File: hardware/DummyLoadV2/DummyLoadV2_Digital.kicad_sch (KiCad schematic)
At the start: 18 parts, among them J1 Conn_01x05_Pin, J2 Fan, Q3 2N7000, Q4 PMOS, SW1 Enable_SW, SW3 Range_SW, U1 Nano

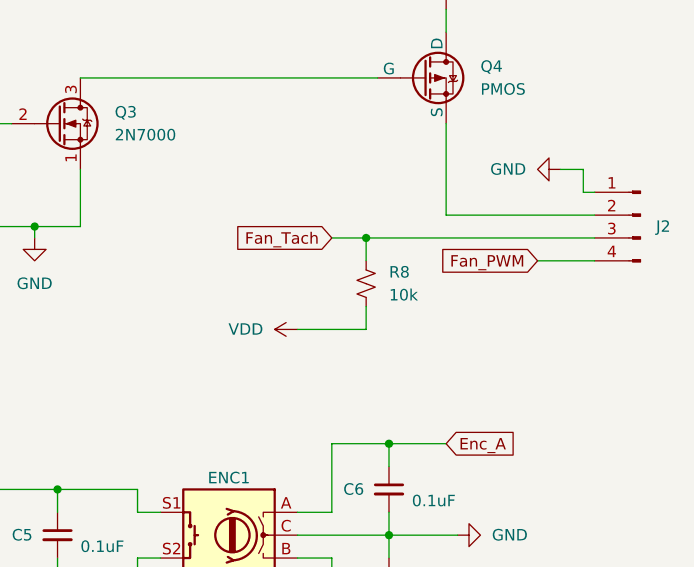
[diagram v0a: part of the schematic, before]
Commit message: Added hardware schematic sheets
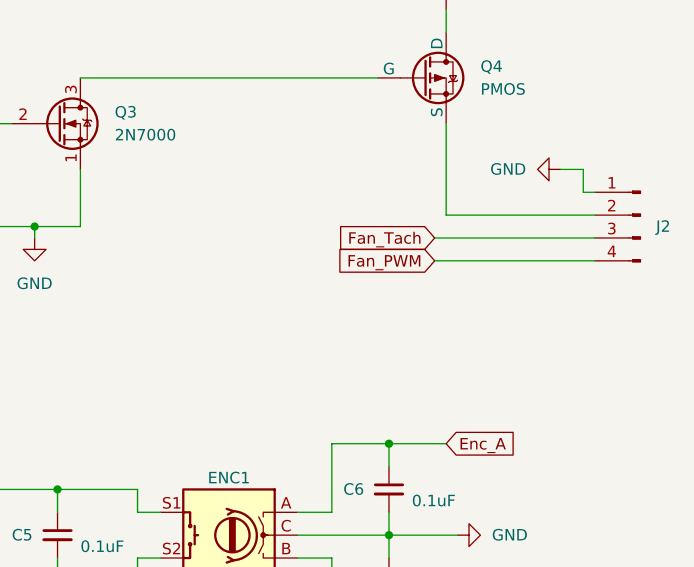
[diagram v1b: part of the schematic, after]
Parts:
- removed R8: 10k, symbol Device:R_Small_US
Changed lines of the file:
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@@
     (rev "1")
-  )
-  (junction (at 217.17 83.82) (diameter 0) (color 0 0 0 0)
   )
   (junction (at 74.93 132.08) (diameter 0) (color 0 0 0 0)
@@
     (stroke (width 0) (type default))
   )
-  (wire (pts (xy 213.36 83.82) (xy 217.17 83.82))
-    (stroke (width 0) (type default))
-  )
   (wire (pts (xy 191.77 111.76) (xy 191.77 114.3))
     (stroke (width 0) (type default))
@@
     (stroke (width 0) (type default))
   )
-  (wire (pts (xy 236.22 86.36) (xy 242.57 86.36))
-    (stroke (width 0) (type default))
-  )
   (wire (pts (xy 50.8 99.06) (xy 60.96 99.06))
     (stroke (width 0) (type default))
@@
     (stroke (width 0) (type default))
   )
-  (wire (pts (xy 217.17 83.82) (xy 217.17 86.36))
-    (stroke (width 0) (type default))
-  )
   (wire (pts (xy 241.3 78.74) (xy 242.57 78.74))
     (stroke (width 0) (type default))
@@
     (stroke (width 0) (type default))
   )
+  (wire (pts (xy 224.79 86.36) (xy 242.57 86.36))
+    (stroke (width 0) (type default))
+  )
   (wire (pts (xy 60.96 114.3) (xy 55.88 114.3))
     (stroke (width 0) (type default))
@@
     (stroke (width 0) (type default))
   )
-  (wire (pts (xy 217.17 83.82) (xy 242.57 83.82))
+  (wire (pts (xy 224.79 83.82) (xy 242.57 83.82))
     (stroke (width 0) (type default))
   )
@@
     (stroke (width 0) (type default))
   )
-  (wire (pts (xy 209.55 93.98) (xy 217.17 93.98))
-    (stroke (width 0) (type default))
-  )
   (wire (pts (xy 33.02 124.46) (xy 46.99 124.46))
     (stroke (width 0) (type default))
@@
   )
   (wire (pts (xy 219.71 116.84) (xy 227.33 116.84))
-    (stroke (width 0) (type default))
-  )
-  (wire (pts (xy 217.17 91.44) (xy 217.17 93.98))
     (stroke (width 0) (type default))
   )
@@
     )
   )
-  (global_label "Fan_PWM" (shape input) (at 236.22 86.36 180) (fields_autoplaced)
+  (global_label "Fan_PWM" (shape input) (at 224.79 86.36 180) (fields_autoplaced)
     (effects (font (size 1.27 1.27)) (justify right))
-    (property "Intersheetrefs" "${INTERSHEET_REFS}" (at 224.7078 86.36 0)
+    (property "Intersheetrefs" "${INTERSHEET_REFS}" (at 213.2778 86.36 0)
       (effects (font (size 1.27 1.27)) (justify right) hide)
     )
@@
     )
   )
-  (global_label "Fan_Tach" (shape input) (at 213.36 83.82 180) (fields_autoplaced)
+  (global_label "Fan_Tach" (shape input) (at 224.79 83.82 180) (fields_autoplaced)
     (effects (font (size 1.27 1.27)) (justify right))
-    (property "Intersheetrefs" "${INTERSHEET_REFS}" (at 201.6664 83.82 0)
+    (property "Intersheetrefs" "${INTERSHEET_REFS}" (at 213.0964 83.82 0)
       (effects (font (size 1.27 1.27)) (justify right) hide)
     )
@@
         (path "/154f9743-c032-4045-ba5f-d157ba47940d/02c25695-dda5-4c86-9b7a-9696a2c46048"
           (reference "NTC") (unit 1)
-        )
-      )
-    )
-  )
-  (symbol (lib_id "Device:R_Small_US") (at 217.17 88.9 0) (unit 1)
-    (in_bom yes) (on_board yes) (dnp no)
-    (property "Reference" "R8" (at 219.71 87.63 0)
-      (effects (font (size 1.27 1.27)) (justify left))
-    )
-    (property "Value" "10k" (at 219.71 90.17 0)
-      (effects (font (size 1.27 1.27)) (justify left))
-    )
-    (property "Footprint" "" (at 217.17 88.9 0)
-      (effects (font (size 1.27 1.27)) hide)
-    )
-    (property "Datasheet" "~" (at 217.17 88.9 0)
-      (effects (font (size 1.27 1.27)) hide)
-    )
-    (pin "1")
-    (pin "2")
-    (instances
-      (project "DummyLoadV2"
-        (path "/154f9743-c032-4045-ba5f-d157ba47940d/02c25695-dda5-4c86-9b7a-9696a2c46048"
-          (reference "R8") (unit 1)
         )
       )
@@
         )
       )
-    )
-  )
-  (symbol (lib_id "power:VDD") (at 209.55 93.98 90) (unit 1)
-    (in_bom yes) (on_board yes) (dnp no)
-    (property "Reference" "#PWR031" (at 213.36 93.98 0)
-      (effects (font (size 1.27 1.27)) hide)
-    )
-    (property "Value" "VDD" (at 205.74 93.98 90)
-      (effects (font (size 1.27 1.27)) (justify left))
-    )
-    (property "Footprint" "" (at 209.55 93.98 0)
-      (effects (font (size 1.27 1.27)) hide)
-    )
-    (property "Datasheet" "" (at 209.55 93.98 0)
-      (effects (font (size 1.27 1.27)) hide)
-    )
-    (pin "1")
-    (instances
-      (project "DummyLoadV2"
-        (path "/154f9743-c032-4045-ba5f-d157ba47940d/02c25695-dda5-4c86-9b7a-9696a2c46048"
-          (reference "#PWR031") (unit 1)
-        )
-      )

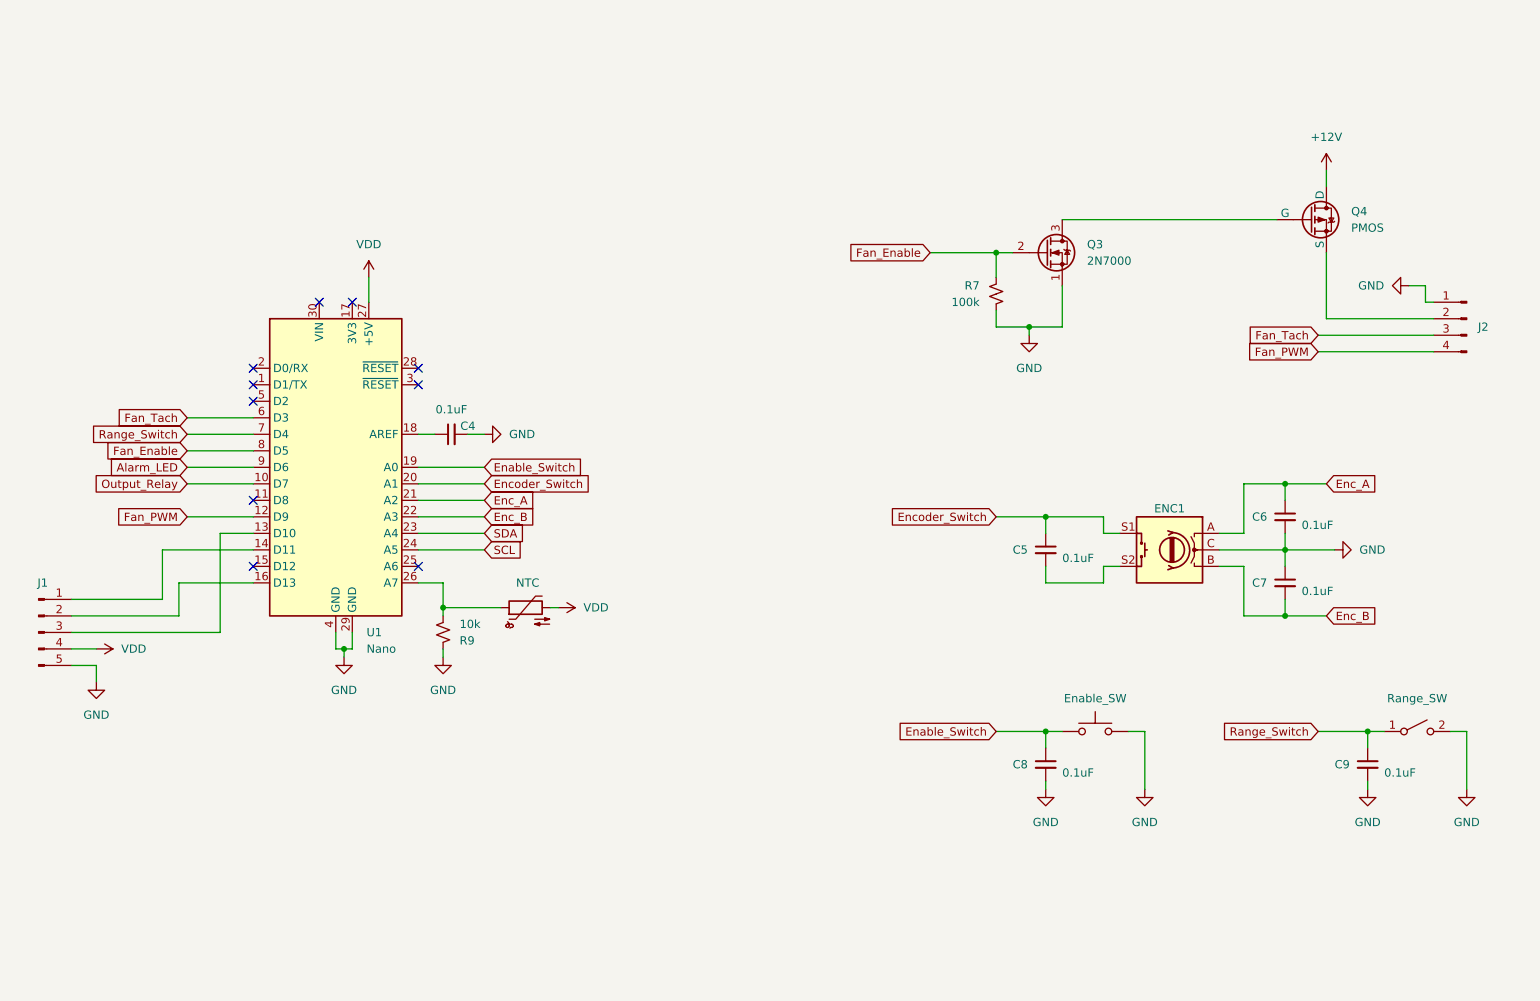
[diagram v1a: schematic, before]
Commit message: Updated pin mapping in schematic
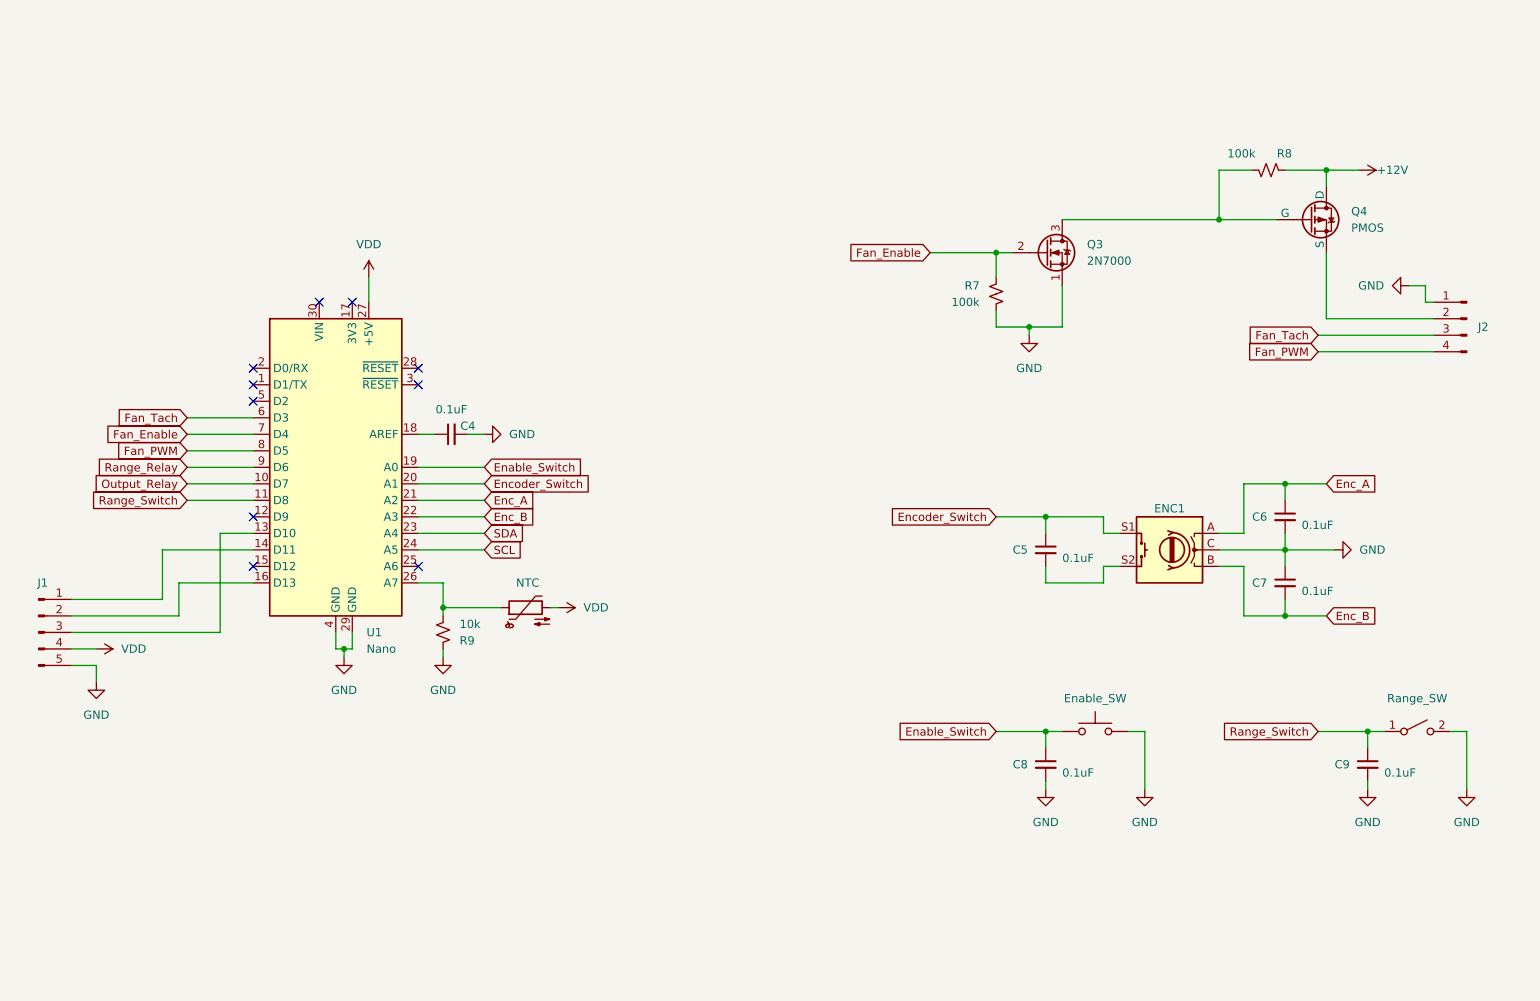
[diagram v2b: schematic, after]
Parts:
- added R8: 100k, symbol Device:R_Small_US
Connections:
- net +12V: now also R8.1
- net Fan_Enable: now also U1.7 (D4); no longer U1.8 (D5)
- net Fan_PWM: now also U1.8 (D5); no longer U1.12 (D9)
- net Range_Switch: now also U1.11 (D8); no longer U1.7 (D4)
- net at Q3.3 (D), Q4.2 (G): now also R8.2
- net Alarm_LED renamed Range_Relay
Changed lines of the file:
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@@
     (rev "1")
   )
+  (junction (at 209.55 66.04) (diameter 0) (color 0 0 0 0)
+  )
   (junction (at 74.93 132.08) (diameter 0) (color 0 0 0 0)
   )
@@
   (junction (at 182.88 111.76) (diameter 0) (color 0 0 0 0)
   )
+  (junction (at 226.06 58.42) (diameter 0) (color 0 0 0 0)
+  )
   (junction (at 182.88 144.78) (diameter 0) (color 0 0 0 0)
   )
@@
   )
   (no_connect (at 86.36 91.44))
+  (no_connect (at 60.96 111.76))
   (no_connect (at 71.12 78.74))
   (no_connect (at 86.36 88.9))
@@
   (no_connect (at 60.96 93.98))
   (no_connect (at 60.96 88.9))
-  (no_connect (at 60.96 109.22))
   (no_connect (at 76.2 78.74))
   (no_connect (at 86.36 119.38))
@@
     (stroke (width 0) (type default))
   )
-  (wire (pts (xy 50.8 111.76) (xy 60.96 111.76))
-    (stroke (width 0) (type default))
-  )
   (wire (pts (xy 180.34 82.55) (xy 185.42 82.55))
     (stroke (width 0) (type default))
@@
     (stroke (width 0) (type default))
   )
+  (wire (pts (xy 50.8 109.22) (xy 60.96 109.22))
+    (stroke (width 0) (type default))
+  )
   (wire (pts (xy 209.55 116.84) (xy 219.71 116.84))
     (stroke (width 0) (type default))
@@
     (stroke (width 0) (type default))
   )
+  (wire (pts (xy 209.55 66.04) (xy 218.44 66.04))
+    (stroke (width 0) (type default))
+  )
   (wire (pts (xy 241.3 78.74) (xy 242.57 78.74))
     (stroke (width 0) (type default))
@@
     (stroke (width 0) (type default))
   )
+  (wire (pts (xy 209.55 58.42) (xy 209.55 66.04))
+    (stroke (width 0) (type default))
+  )
+  (wire (pts (xy 219.71 58.42) (xy 226.06 58.42))
+    (stroke (width 0) (type default))
+  )
   (wire (pts (xy 60.96 114.3) (xy 55.88 114.3))
     (stroke (width 0) (type default))
@@
     (stroke (width 0) (type default))
   )
+  (wire (pts (xy 209.55 58.42) (xy 214.63 58.42))
+    (stroke (width 0) (type default))
+  )
   (wire (pts (xy 86.36 99.06) (xy 88.9 99.06))
     (stroke (width 0) (type default))
@@
     (stroke (width 0) (type default))
   )
+  (wire (pts (xy 231.14 58.42) (xy 226.06 58.42))
+    (stroke (width 0) (type default))
+  )
   (wire (pts (xy 33.02 124.46) (xy 46.99 124.46))
     (stroke (width 0) (type default))
@@
     (stroke (width 0) (type default))
   )
-  (wire (pts (xy 185.42 66.04) (xy 218.44 66.04))
+  (wire (pts (xy 185.42 66.04) (xy 209.55 66.04))
     (stroke (width 0) (type default))
   )
@@
     )
   )
-  (global_label "Alarm_LED" (shape input) (at 50.8 104.14 180) (fields_autoplaced)
-    (effects (font (size 1.27 1.27)) (justify right))
-    (property "Intersheetrefs" "${INTERSHEET_REFS}" (at 38.0178 104.14 0)
+  (global_label "Range_Relay" (shape input) (at 50.8 104.14 180) (fields_autoplaced)
+    (effects (font (size 1.27 1.27)) (justify right))
+    (property "Intersheetrefs" "${INTERSHEET_REFS}" (at 35.9012 104.14 0)
       (effects (font (size 1.27 1.27)) (justify right) hide)
     )
@@
     )
   )
-  (global_label "Range_Switch" (shape input) (at 50.8 99.06 180) (fields_autoplaced)
-    (effects (font (size 1.27 1.27)) (justify right))
-    (property "Intersheetrefs" "${INTERSHEET_REFS}" (at 34.9335 99.06 0)
+  (global_label "Range_Switch" (shape input) (at 50.8 109.22 180) (fields_autoplaced)
+    (effects (font (size 1.27 1.27)) (justify right))
+    (property "Intersheetrefs" "${INTERSHEET_REFS}" (at 34.9335 109.22 0)
       (effects (font (size 1.27 1.27)) (justify right) hide)
     )
@@
     )
   )
-  (global_label "Fan_PWM" (shape input) (at 50.8 111.76 180) (fields_autoplaced)
-    (effects (font (size 1.27 1.27)) (justify right))
-    (property "Intersheetrefs" "${INTERSHEET_REFS}" (at 39.2878 111.76 0)
-      (effects (font (size 1.27 1.27)) (justify right) hide)
-    )
-  )
-  (global_label "Fan_Enable" (shape input) (at 50.8 101.6 180) (fields_autoplaced)
-    (effects (font (size 1.27 1.27)) (justify right))
-    (property "Intersheetrefs" "${INTERSHEET_REFS}" (at 37.1108 101.6 0)
+  (global_label "Fan_PWM" (shape input) (at 50.8 101.6 180) (fields_autoplaced)
+    (effects (font (size 1.27 1.27)) (justify right))
+    (property "Intersheetrefs" "${INTERSHEET_REFS}" (at 39.2878 101.6 0)
+      (effects (font (size 1.27 1.27)) (justify right) hide)
+    )
+  )
+  (global_label "Fan_Enable" (shape input) (at 50.8 99.06 180) (fields_autoplaced)
+    (effects (font (size 1.27 1.27)) (justify right))
+    (property "Intersheetrefs" "${INTERSHEET_REFS}" (at 37.1108 99.06 0)
       (effects (font (size 1.27 1.27)) (justify right) hide)
     )
@@
     )
   )
-  (symbol (lib_id "power:+12V") (at 226.06 58.42 0) (unit 1)
+  (symbol (lib_id "power:+12V") (at 231.14 58.42 270) (unit 1)
     (in_bom yes) (on_board yes) (dnp no)
-    (property "Reference" "#PWR029" (at 226.06 62.23 0)
-      (effects (font (size 1.27 1.27)) hide)
-    )
-    (property "Value" "+12V" (at 226.06 53.34 0)
-      (effects (font (size 1.27 1.27)))
-    )
-    (property "Footprint" "" (at 226.06 58.42 0)
-      (effects (font (size 1.27 1.27)) hide)
-    )
-    (property "Datasheet" "" (at 226.06 58.42 0)
+    (property "Reference" "#PWR029" (at 227.33 58.42 0)
+      (effects (font (size 1.27 1.27)) hide)
+    )
+    (property "Value" "+12V" (at 236.22 58.42 90)
+      (effects (font (size 1.27 1.27)))
+    )
+    (property "Footprint" "" (at 231.14 58.42 0)
+      (effects (font (size 1.27 1.27)) hide)
+    )
+    (property "Datasheet" "" (at 231.14 58.42 0)
       (effects (font (size 1.27 1.27)) hide)
     )
@@
         )
       )
+    )
+  )
+  (symbol (lib_id "Device:R_Small_US") (at 217.17 58.42 270) (mirror x) (unit 1)
+    (in_bom yes) (on_board yes) (dnp no)
+    (property "Reference" "R8" (at 218.44 55.88 90)
+      (effects (font (size 1.27 1.27)) (justify left))
+    )
+    (property "Value" "100k" (at 210.82 55.88 90)
+      (effects (font (size 1.27 1.27)) (justify left))
+    )
+    (property "Footprint" "" (at 217.17 58.42 0)
+      (effects (font (size 1.27 1.27)) hide)
+    )
+    (property "Datasheet" "~" (at 217.17 58.42 0)
+      (effects (font (size 1.27 1.27)) hide)
+    )
+    (pin "1")
+    (pin "2")
+    (instances
+      (project "DummyLoadV2"
+        (path "/154f9743-c032-4045-ba5f-d157ba47940d/02c25695-dda5-4c86-9b7a-9696a2c46048"
+          (reference "R8") (unit 1)
+        )
+      )

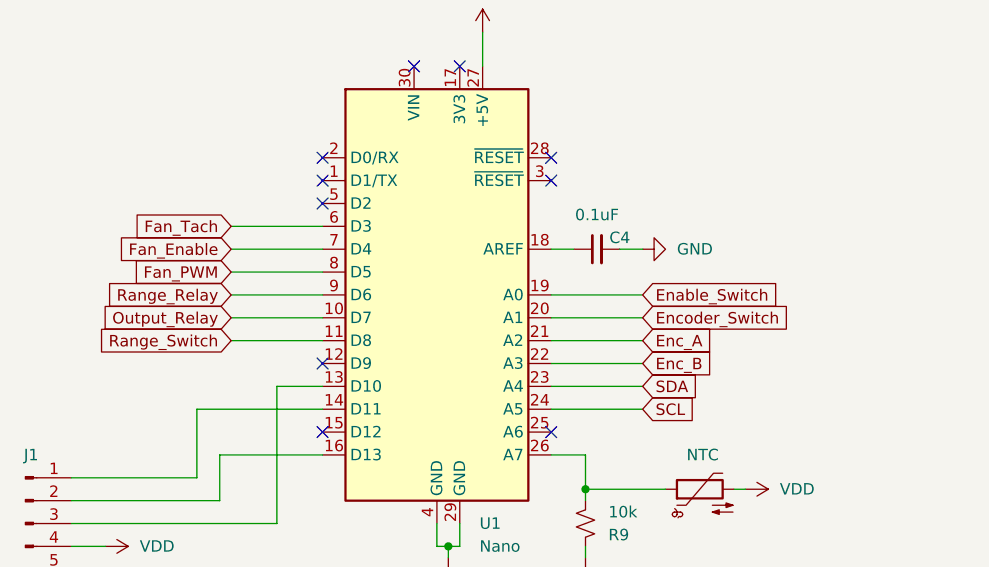
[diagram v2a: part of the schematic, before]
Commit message: Moved pins around for easier wiring
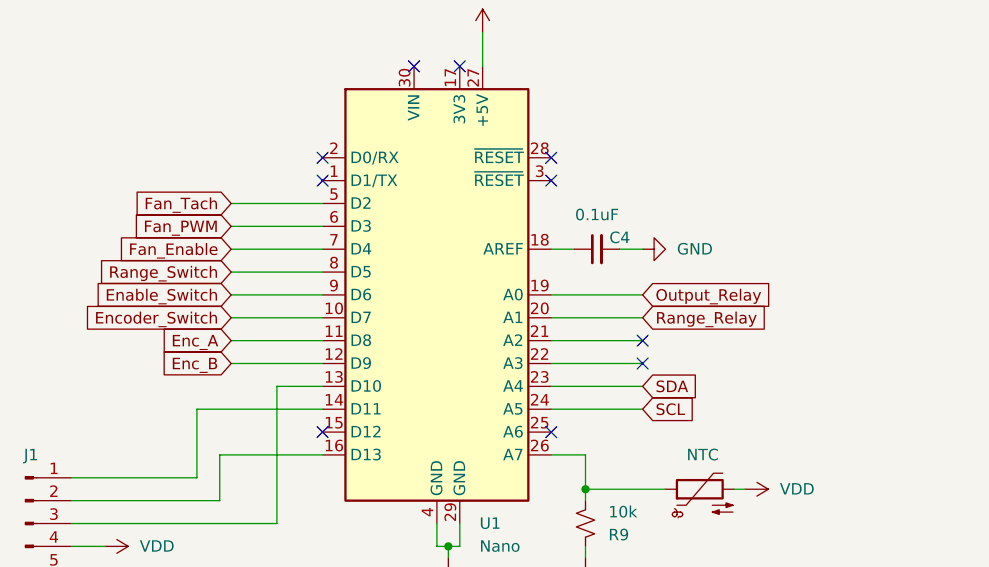
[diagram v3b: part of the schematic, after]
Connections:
- net Enable_Switch: now also U1.9 (D6); no longer U1.19 (A0)
- net Enc_A: now also U1.11 (D8); no longer U1.21 (A2)
- net Enc_B: now also U1.12 (D9); no longer U1.22 (A3)
- net Encoder_Switch: now also U1.10 (D7); no longer U1.20 (A1)
- net Fan_PWM: now also U1.6 (D3); no longer U1.8 (D5)
- net Fan_Tach: now also U1.5 (D2); no longer U1.6 (D3)
- net Output_Relay: now also U1.19 (A0); no longer U1.10 (D7)
- net Range_Relay: now also U1.20 (A1); no longer U1.9 (D6)
- net Range_Switch: now also U1.8 (D5); no longer U1.11 (D8)
